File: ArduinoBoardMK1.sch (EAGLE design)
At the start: 26 parts, among them IC1 TLE5205-2, K1 G5LE, K2 G5LE, K3 G5LE, T1 2N3704, T2 2N3704, T3 2N3704

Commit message: ArduinoBaord MK1 Schematic Complete
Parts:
- removed D1, D3: 1N4004, diode:1N4004
- removed FAN, PUMP: SMKDSP_1,5/2, con-phoenix-smkdsp:SMKDSP_1,5/2
- removed K1, K3: G5LE, relay:G5LE
- removed R4, R5, R6: (no value), resistor:R-US_0207/12
- removed T1, T2, T3: 2N3704, transistor:2N3704
- added 12V, DOOR, VIN: SMKDSP_1,5/2, con-phoenix-smkdsp:SMKDSP_1,5/2
- added J1: (no value), SparkFun-Connectors:CONN_03LONGPADS
- added OK1: PC817, optocoupler:PC817
- added X1: 22-23-2021, con-molex:22-23-2021
- R1, R2: value (none) -> 220
- R10, R9: value (none) -> 47k
- R3: value (none) -> 4.7k
- R7, R8: value (none) -> 1k
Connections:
- removed net C2: R2.1
- removed net N$11: K32.P, PUMP-1.KL
- removed net N$12: R4.2, R5.2, T3.B
- removed net N$2: D1.A, K11.2, T1.C
- removed net N$23: U$1.A0
- removed net N$24: U$1.A1
- removed net N$8: R2.2, R6.2, T2.B
- removed net N$9: D3.A, K31.2, T3.C
- new net DOORSWITCH: DOOR-2.KL, R3.1, U$1.A2
- new net MOTOR-ENABLE: OK1.A, U$1.IO9*
- new net MOTOR-ERRORFLAG: IC1.EF, U$1.IO12*
- new net N$21: U$1.D7
- new net N$22: U$1.IO8
- new net SCL: U$1.D3/SCL, X1-2.S
- new net SDA: U$1.D2/SDA, X1-1.S
- new net TEMPERATURE: J1.2, U$1.A1
- new net VIN: U$1.VIN, VIN-1.KL
- net +12V: now also 12V-1.KL, R2.2; no longer D1.C, D2.C, D3.C, K11.1, K12.S, K21.1, K31.1, K32.S
- net +5V: now also DOOR-1.KL, J1.3
- net GND: now also 12V-2.KL, J1.1, OK1.EMIT, R1.1, R3.2, U$1.GND, U$1.GND1, VIN-2.KL; no longer FAN-2.KL, PUMP-2.KL, R3.1, R4.1, R6.1, T1.E, T2.E, T3.E
- net MOTOR-IN1: now also U$1.IO10*
- net MOTOR-IN2: now also U$1.IO11*
- net N$1: now also OK1.C; no longer R3.2, T1.B
- net N$16: now also PELTIER1-1.KL; no longer PELTIER1-2.KL
- net N$17: now also PELTIER1-2.KL; no longer PELTIER1-1.KL
- net N$3: now also OK1.COL; no longer T2.C
- net N$5: now also D2.C, K21.1, R2.1; no longer FAN-1.KL, K12.P
- net PELTIER-CURRENT: now also U$1.A0
- net PELTIER-INA: now also U$1.D6*
- net PELTIER-INB: now also U$1.D4*
- net PELTIER-PWM: now also U$1.D5*
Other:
- note added: "4 and 12 may not have PWM"
- moved on the sheet: PELTIER1-1, PELTIER1-2, R1, R2, R3, R7, U$1

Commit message: Arduino Board PCB Layout
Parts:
- removed DOOR: SMKDSP_1,5/2, con-phoenix-smkdsp:SMKDSP_1,5/2
- removed X1: 22-23-2021, con-molex:22-23-2021
- added SDA__SCL, SWITCH: (no value), SparkFun-Connectors:CONN_02PTH3
- renumbered IC1 to TLE5205, K2 to RELAY, U$1 to MICRO, U$2 to VNH5019
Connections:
- net +5V: now also SWITCH.2; no longer DOOR-1.KL
- net DOORSWITCH: now also SWITCH.1; no longer DOOR-2.KL
- net SCL: now also SDA__SCL.2; no longer X1-2.S
- net SDA: now also SDA__SCL.1; no longer X1-1.S

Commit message: Updated PCB VIAS +more
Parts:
- added R11, R6: 47k, resistor:R-US_0207/12
- added SDA__SCL1: (no value), SparkFun-Connectors:CONN_02PTH3
- added TEMPERATURE2: (no value), SparkFun-Connectors:CONN_03LONGPADS
- renumbered J1 to TEMPERATURE1, OK1 to PC817, SDA__SCL to SDA__SCL2
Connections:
- net TEMPERATURE renamed TEMPERATURE1
- removed net N$14: VNH5019.ENA
- removed net N$18: VNH5019.ENB
- new net TEMPERATURE2: MICRO.A5, TEMPERATURE2.2
- net +5V: now also TEMPERATURE2.3
- net GND: now also R11.2, R6.1, TEMPERATURE2.1
- net PELTIER-INA: now also R11.1
- net PELTIER-INB: now also R6.2
- net SCL: now also SDA__SCL1.2
- net SDA: now also SDA__SCL1.1
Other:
- moved on the sheet: MOTOR1-1, MOTOR1-2, R7

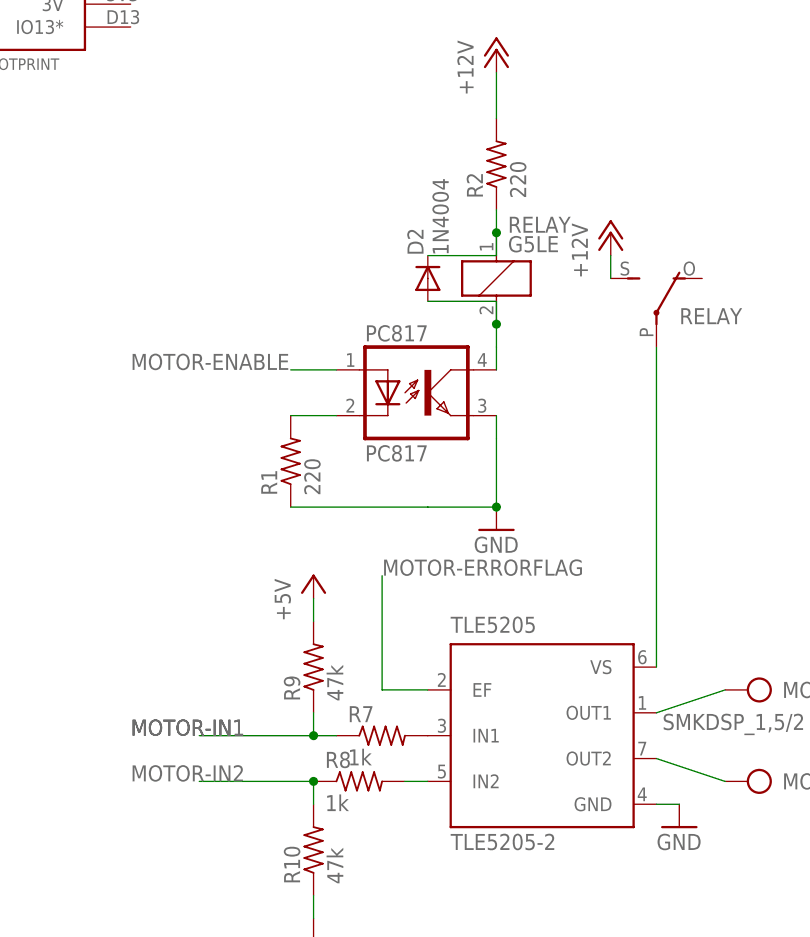
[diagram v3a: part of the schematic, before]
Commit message: Net Lables + Pull-Down Resistors on Electron
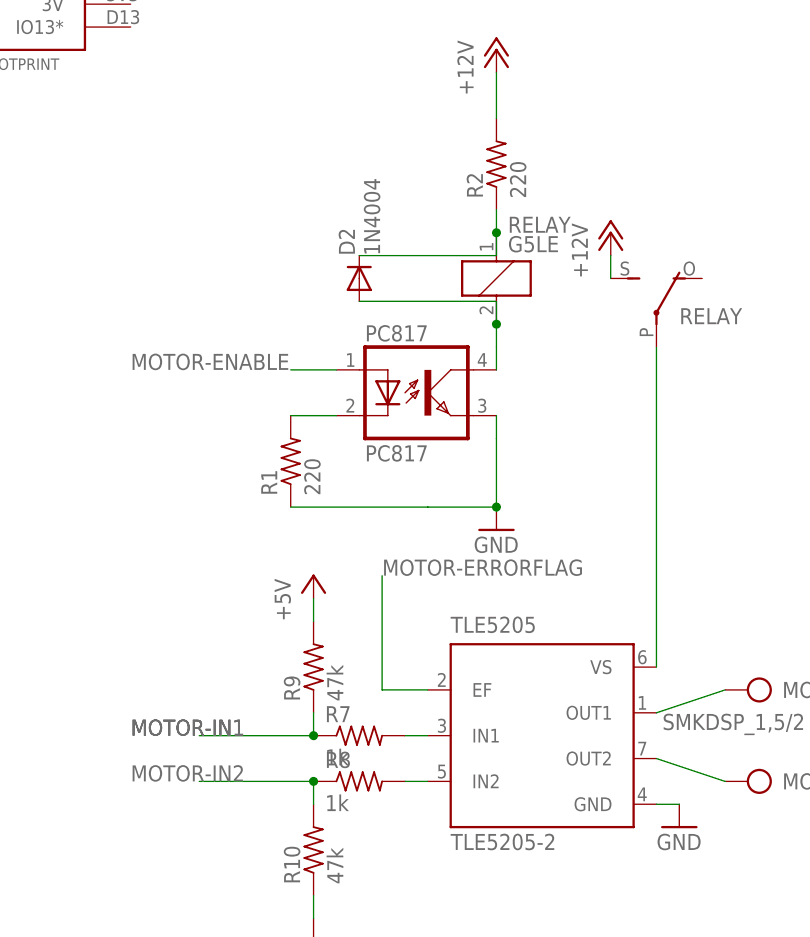
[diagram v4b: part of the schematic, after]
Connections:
- net N$1 renamed POST-OPTO-DIODE
- net N$10 renamed IN1
- net N$13 renamed IN2
- net N$16 renamed PELTIER-OUTB
- net N$17 renamed PELTIER-OUTA
- net N$3 renamed RELAY-TO-OPTO
- net N$4 renamed RELAY-TO-MOTORCONTROLLER
- net N$5 renamed FLYBACK-DIODE+
- net N$6 renamed MOTOR-OUT1
- net N$7 renamed MOTOR-OUT2
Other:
- moved on the sheet: D2, R7
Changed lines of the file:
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@@
 <instance part="TLE5205" gate="G$1" x="12.7" y="-43.18"/>
 <instance part="GND1" gate="1" x="27.94" y="-53.34"/>
-<instance part="R7" gate="G$1" x="-5.08" y="-43.18"/>
+<instance part="R7" gate="G$1" x="-7.62" y="-43.18"/>
 <instance part="R8" gate="G$1" x="-7.62" y="-48.26"/>
 <instance part="RELAY" gate="1" x="7.62" y="7.62"/>
 <instance part="RELAY" gate="2" x="25.4" y="2.54"/>
-<instance part="D2" gate="1" x="0" y="7.62" rot="R90"/>
+<instance part="D2" gate="1" x="-7.62" y="7.62" rot="R90"/>
 <instance part="GND4" gate="1" x="7.62" y="-20.32"/>
 <instance part="P+4" gate="1" x="20.32" y="12.7"/>
@@
 </segment>
 </net>
-<net name="N$3" class="0">
+<net name="RELAY-TO-OPTO" class="0">
 <segment>
 <pinref part="RELAY" gate="1" pin="2"/>
 <pinref part="D2" gate="1" pin="A"/>
-<wire x1="0" y1="5.08" x2="7.62" y2="5.08" width="0.1524" layer="91"/>
+<wire x1="-7.62" y1="5.08" x2="7.62" y2="5.08" width="0.1524" layer="91"/>
 <wire x1="7.62" y1="5.08" x2="7.62" y2="2.54" width="0.1524" layer="91"/>
 <wire x1="7.62" y1="2.54" x2="7.62" y2="0" width="0.1524" layer="91"/>
@@
 </segment>
 </net>
-<net name="N$4" class="0">
+<net name="RELAY-TO-MOTORCONTROLLER" class="0">
 <segment>
 <pinref part="TLE5205" gate="G$1" pin="VS"/>
@@
 </segment>
 </net>
-<net name="N$10" class="0">
+<net name="IN1" class="0">
 <segment>
 <pinref part="TLE5205" gate="G$1" pin="IN1"/>
 <pinref part="R7" gate="G$1" pin="2"/>
-</segment>
-</net>
-<net name="N$13" class="0">
+<wire x1="-2.54" y1="-43.18" x2="0" y2="-43.18" width="0.1524" layer="91"/>
+</segment>
+</net>
+<net name="IN2" class="0">
 <segment>
 <pinref part="TLE5205" gate="G$1" pin="IN2"/>
@@
 </segment>
 </net>
-<net name="N$6" class="0">
+<net name="MOTOR-OUT1" class="0">
 <segment>
 <pinref part="TLE5205" gate="G$1" pin="OUT1"/>
@@
 </segment>
 </net>
-<net name="N$7" class="0">
+<net name="MOTOR-OUT2" class="0">
 <segment>
 <pinref part="TLE5205" gate="G$1" pin="OUT2"/>
@@
 <segment>
 <pinref part="R7" gate="G$1" pin="1"/>
-<wire x1="-10.16" y1="-43.18" x2="-12.7" y2="-43.18" width="0.1524" layer="91"/>
 <label x="-33.02" y="-43.18" size="1.778" layer="95"/>
 <label x="-33.02" y="-43.18" size="1.778" layer="95"/>
@@
 </segment>
 </net>
-<net name="N$16" class="0">
+<net name="PELTIER-OUTB" class="0">
 <segment>
 <pinref part="VNH5019" gate="G$1" pin="OUTB2"/>
@@
 </segment>
 </net>
-<net name="N$17" class="0">
+<net name="PELTIER-OUTA" class="0">
 <segment>
 <pinref part="VNH5019" gate="G$1" pin="OUTA2"/>
@@
 </segment>
 </net>
-<net name="N$1" class="0">
+<net name="POST-OPTO-DIODE" class="0">
 <segment>
 <pinref part="R1" gate="G$1" pin="2"/>
@@
 </segment>
 </net>
-<net name="N$5" class="0">
+<net name="FLYBACK-DIODE+" class="0">
 <segment>
 <pinref part="RELAY" gate="1" pin="1"/>
 <pinref part="D2" gate="1" pin="C"/>
-<wire x1="0" y1="10.16" x2="7.62" y2="10.16" width="0.1524" layer="91"/>
+<wire x1="-7.62" y1="10.16" x2="7.62" y2="10.16" width="0.1524" layer="91"/>
 <wire x1="7.62" y1="10.16" x2="7.62" y2="12.7" width="0.1524" layer="91"/>
 <pinref part="R2" gate="G$1" pin="1"/>

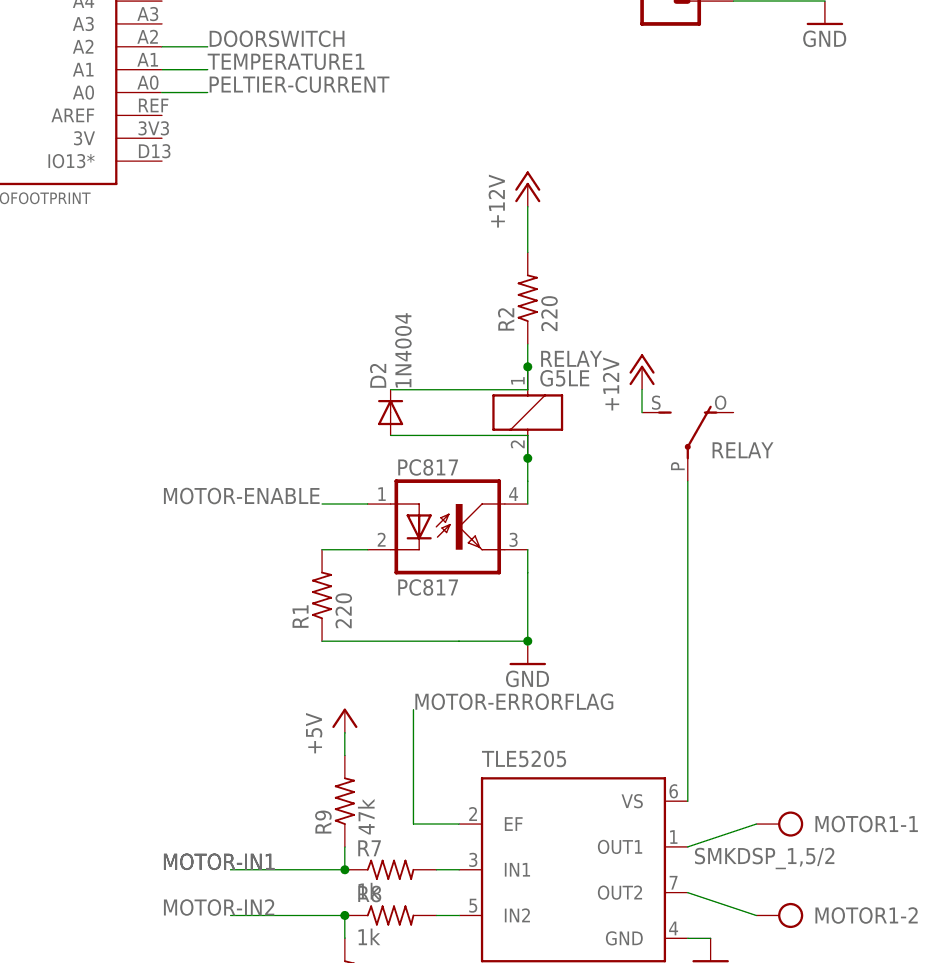
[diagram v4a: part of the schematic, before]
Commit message: Solid State Relay
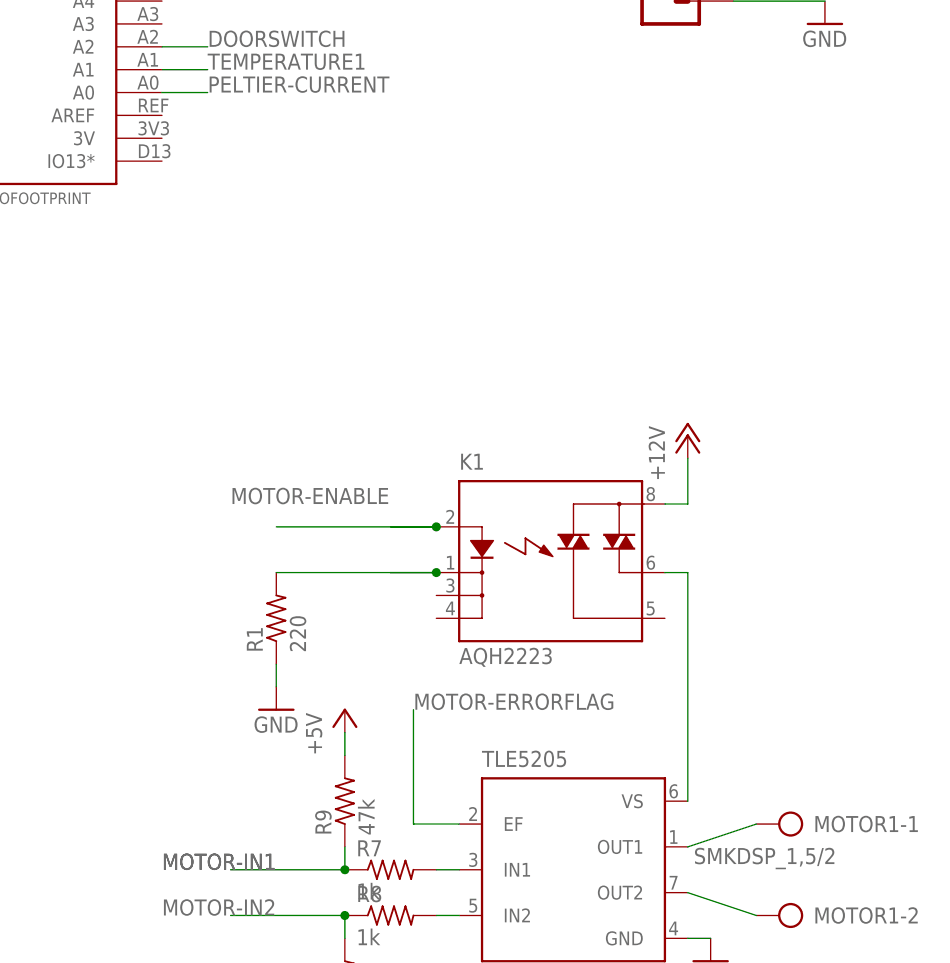
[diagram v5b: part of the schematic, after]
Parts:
- removed D2: 1N4004, diode:1N4004
- removed PC817: PC817, optocoupler:PC817
- removed R2: 220, resistor:R-US_0207/12
- removed RELAY: G5LE, relay:G5LE
- added K1: AQH2223, relay:AQH2223
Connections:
- removed net FLYBACK-DIODE+: D2.C, R2.1, RELAY1.1
- removed net RELAY-TO-OPTO: D2.A, PC817.COL, RELAY1.2
- net +12V: now also K1.DS1; no longer R2.2, RELAY2.S
- net GND: no longer PC817.EMIT
- net MOTOR-ENABLE: now also K1.A; no longer PC817.A
- net POST-OPTO-DIODE: now also K1.K; no longer PC817.C
- net RELAY-TO-MOTORCONTROLLER: now also K1.DS3; no longer RELAY2.P
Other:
- moved on the sheet: R1
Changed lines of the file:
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@@
 <part name="R7" library="resistor" library_urn="urn:adsk.eagle:library:348" deviceset="R-US_" device="0207/12" package3d_urn="urn:adsk.eagle:package:25938/1" value="1k"/>
 <part name="R8" library="resistor" library_urn="urn:adsk.eagle:library:348" deviceset="R-US_" device="0207/12" package3d_urn="urn:adsk.eagle:package:25938/1" value="1k"/>
-<part name="RELAY" library="relay" library_urn="urn:adsk.eagle:library:339" deviceset="G5LE" device="" package3d_urn="urn:adsk.eagle:package:24308/1"/>
-<part name="D2" library="diode" library_urn="urn:adsk.eagle:library:210" deviceset="1N4004" device="" package3d_urn="urn:adsk.eagle:package:43336/1"/>
 <part name="GND4" library="supply1" library_urn="urn:adsk.eagle:library:371" deviceset="GND" device=""/>
 <part name="P+4" library="supply1" library_urn="urn:adsk.eagle:library:371" deviceset="+12V" device=""/>
-<part name="P+7" library="supply1" library_urn="urn:adsk.eagle:library:371" deviceset="+12V" device=""/>
 <part name="MOTOR1" library="con-phoenix-smkdsp" library_urn="urn:adsk.eagle:library:180" deviceset="SMKDSP_1,5/2" device="" package3d_urn="urn:adsk.eagle:package:9814/1"/>
 <part name="P+8" library="supply1" library_urn="urn:adsk.eagle:library:371" deviceset="+12V" device=""/>
@@
 <part name="VIN" library="con-phoenix-smkdsp" library_urn="urn:adsk.eagle:library:180" deviceset="SMKDSP_1,5/2" device="" package3d_urn="urn:adsk.eagle:package:9814/1"/>
 <part name="P+1" library="supply1" library_urn="urn:adsk.eagle:library:371" deviceset="+12V" device=""/>
-<part name="PC817" library="optocoupler" library_urn="urn:adsk.eagle:library:320" deviceset="PC817" device="" package3d_urn="urn:adsk.eagle:package:21938/1"/>
 <part name="R1" library="resistor" library_urn="urn:adsk.eagle:library:348" deviceset="R-US_" device="0207/12" package3d_urn="urn:adsk.eagle:package:25938/1" value="220"/>
-<part name="R2" library="resistor" library_urn="urn:adsk.eagle:library:348" deviceset="R-US_" device="0207/12" package3d_urn="urn:adsk.eagle:package:25938/1" value="220"/>
 <part name="GND2" library="supply1" library_urn="urn:adsk.eagle:library:371" deviceset="GND" device=""/>
 <part name="GND3" library="supply1" library_urn="urn:adsk.eagle:library:371" deviceset="GND" device=""/>
@@
 <part name="GND13" library="supply1" library_urn="urn:adsk.eagle:library:371" deviceset="GND" device=""/>
 <part name="GND14" library="supply1" library_urn="urn:adsk.eagle:library:371" deviceset="GND" device=""/>
+<part name="K1" library="relay" library_urn="urn:adsk.eagle:library:339" deviceset="AQH*223" device="" package3d_urn="urn:adsk.eagle:package:24378/1" technology="2"/>
 </parts>
 <sheets>
@@
 <instance part="R7" gate="G$1" x="-7.62" y="-43.18"/>
 <instance part="R8" gate="G$1" x="-7.62" y="-48.26"/>
-<instance part="RELAY" gate="1" x="7.62" y="7.62"/>
-<instance part="RELAY" gate="2" x="25.4" y="2.54"/>
-<instance part="D2" gate="1" x="-7.62" y="7.62" rot="R90"/>
-<instance part="GND4" gate="1" x="7.62" y="-20.32"/>
-<instance part="P+4" gate="1" x="20.32" y="12.7"/>
-<instance part="P+7" gate="1" x="7.62" y="33.02"/>
+<instance part="GND4" gate="1" x="-20.32" y="-25.4"/>
+<instance part="P+4" gate="1" x="25.4" y="5.08"/>
 <instance part="MOTOR1" gate="-1" x="38.1" y="-38.1" rot="R180"/>
 <instance part="MOTOR1" gate="-2" x="38.1" y="-48.26" rot="R180"/>
@@
 <instance part="VIN" gate="-2" x="99.06" y="-5.08" rot="R180"/>
 <instance part="P+1" gate="1" x="78.74" y="-33.02" rot="R90"/>
-<instance part="PC817" gate="A" x="0" y="-5.08"/>
-<instance part="R1" gate="G$1" x="-15.24" y="-12.7" rot="R90"/>
-<instance part="R2" gate="G$1" x="7.62" y="20.32" rot="R90"/>
+<instance part="R1" gate="G$1" x="-20.32" y="-15.24" rot="R90"/>
 <instance part="GND2" gate="1" x="86.36" y="-7.62"/>
 <instance part="GND3" gate="1" x="127" y="-71.12"/>
@@
 <instance part="GND13" gate="1" x="58.42" y="-83.82"/>
 <instance part="GND14" gate="1" x="66.04" y="-48.26"/>
+<instance part="K1" gate="G$1" x="10.16" y="-10.16"/>
 </instances>
 <busses>
@@
 <segment>
 <pinref part="GND4" gate="1" pin="GND"/>
-<wire x1="7.62" y1="-10.16" x2="7.62" y2="-17.78" width="0.1524" layer="91"/>
-<wire x1="0" y1="-17.78" x2="7.62" y2="-17.78" width="0.1524" layer="91"/>
-<junction x="7.62" y="-17.78"/>
-<pinref part="PC817" gate="A" pin="EMIT"/>
-<wire x1="7.62" y1="-7.62" x2="7.62" y2="-10.16" width="0.1524" layer="91"/>
 <pinref part="R1" gate="G$1" pin="1"/>
-<wire x1="-15.24" y1="-17.78" x2="0" y2="-17.78" width="0.1524" layer="91"/>
+<wire x1="-20.32" y1="-20.32" x2="-20.32" y2="-22.86" width="0.1524" layer="91"/>
 </segment>
 <segment>
@@
 <net name="+12V" class="0">
 <segment>
-<pinref part="RELAY" gate="2" pin="S"/>
-<pinref part="P+4" gate="1" pin="+12V"/>
-<wire x1="20.32" y1="7.62" x2="20.32" y2="10.16" width="0.1524" layer="91"/>
-</segment>
-<segment>
 <pinref part="VNH5019" gate="G$1" pin="VIN2"/>
 <pinref part="VNH5019" gate="G$1" pin="VIN1"/>
@@
 </segment>
 <segment>
-<pinref part="R2" gate="G$1" pin="2"/>
-<pinref part="P+7" gate="1" pin="+12V"/>
-<wire x1="7.62" y1="25.4" x2="7.62" y2="30.48" width="0.1524" layer="91"/>
-</segment>
-</net>
-<net name="RELAY-TO-OPTO" class="0">
-<segment>
-<pinref part="RELAY" gate="1" pin="2"/>
-<pinref part="D2" gate="1" pin="A"/>
-<wire x1="-7.62" y1="5.08" x2="7.62" y2="5.08" width="0.1524" layer="91"/>
-<wire x1="7.62" y1="5.08" x2="7.62" y2="2.54" width="0.1524" layer="91"/>
-<wire x1="7.62" y1="2.54" x2="7.62" y2="0" width="0.1524" layer="91"/>
-<junction x="7.62" y="2.54"/>
-<pinref part="PC817" gate="A" pin="COL"/>
-<wire x1="7.62" y1="-2.54" x2="7.62" y2="0" width="0.1524" layer="91"/>
+<pinref part="P+4" gate="1" pin="+12V"/>
+<wire x1="22.86" y1="-2.54" x2="25.4" y2="-2.54" width="0.1524" layer="91"/>
+<wire x1="25.4" y1="-2.54" x2="25.4" y2="2.54" width="0.1524" layer="91"/>
+<pinref part="K1" gate="G$1" pin="DS1"/>
 </segment>
 </net>
@@
 <segment>
 <pinref part="TLE5205" gate="G$1" pin="VS"/>
-<pinref part="RELAY" gate="2" pin="P"/>
-<wire x1="25.4" y1="-35.56" x2="25.4" y2="0" width="0.1524" layer="91"/>
+<wire x1="25.4" y1="-35.56" x2="25.4" y2="-10.16" width="0.1524" layer="91"/>
+<wire x1="22.86" y1="-10.16" x2="25.4" y2="-10.16" width="0.1524" layer="91"/>
+<pinref part="K1" gate="G$1" pin="DS3"/>
 </segment>
 </net>
@@
 <net name="MOTOR-ENABLE" class="0">
 <segment>
-<wire x1="-10.16" y1="-2.54" x2="-15.24" y2="-2.54" width="0.1524" layer="91"/>
-<label x="-33.02" y="-2.54" size="1.778" layer="95"/>
-<pinref part="PC817" gate="A" pin="A"/>
+<wire x1="-7.62" y1="-5.08" x2="-2.54" y2="-5.08" width="0.1524" layer="91"/>
+<label x="-25.4" y="-2.54" size="1.778" layer="95"/>
+<pinref part="K1" gate="G$1" pin="A"/>
+<wire x1="-2.54" y1="-5.08" x2="-20.32" y2="-5.08" width="0.1524" layer="91"/>
+<junction x="-2.54" y="-5.08"/>
 </segment>
 <segment>
@@
 <segment>
 <pinref part="R1" gate="G$1" pin="2"/>
-<pinref part="PC817" gate="A" pin="C"/>
-<wire x1="-15.24" y1="-7.62" x2="-10.16" y2="-7.62" width="0.1524" layer="91"/>
-</segment>
-</net>
-<net name="FLYBACK-DIODE+" class="0">
-<segment>
-<pinref part="RELAY" gate="1" pin="1"/>
-<pinref part="D2" gate="1" pin="C"/>
-<wire x1="-7.62" y1="10.16" x2="7.62" y2="10.16" width="0.1524" layer="91"/>
-<wire x1="7.62" y1="10.16" x2="7.62" y2="12.7" width="0.1524" layer="91"/>
-<pinref part="R2" gate="G$1" pin="1"/>
-<wire x1="7.62" y1="12.7" x2="7.62" y2="15.24" width="0.1524" layer="91"/>
-<junction x="7.62" y="12.7"/>
-</segment>
-</net>
+<wire x1="-20.32" y1="-10.16" x2="-2.54" y2="-10.16" width="0.1524" layer="91"/>
+<pinref part="K1" gate="G$1" pin="K"/>
+<wire x1="-2.54" y1="-10.16" x2="-7.62" y2="-10.16" width="0.1524" layer="91"/>
+<junction x="-2.54" y="-10.16"/>
+</segment>
+</net>
